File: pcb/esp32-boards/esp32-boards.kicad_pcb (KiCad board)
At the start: 2 copper layers, 55 x 42 mm, 50 parts, among them J1 LCD, J2 USB_B_Micro, J3 BATTERY, Q1 Q_Photo_NPN, SW1 BOOT_MODE, SW2 START, SW3 RESET, SW4 BATTERY_EN, U1 ESP32-C3-WROOM-02, U2 MAX40200AUK, U3 MCP73831-2-OT, U4 LD39150DT33

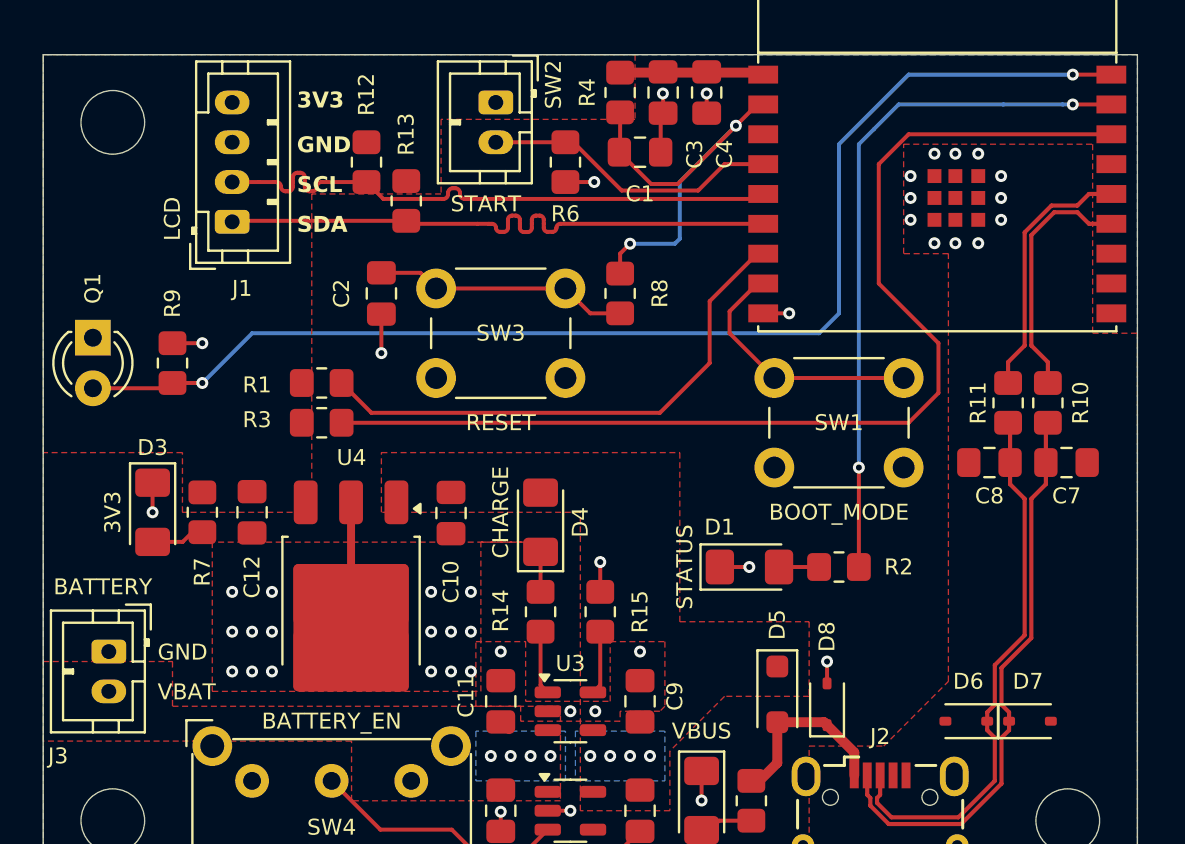
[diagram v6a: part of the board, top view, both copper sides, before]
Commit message: add final touches on silkscreen
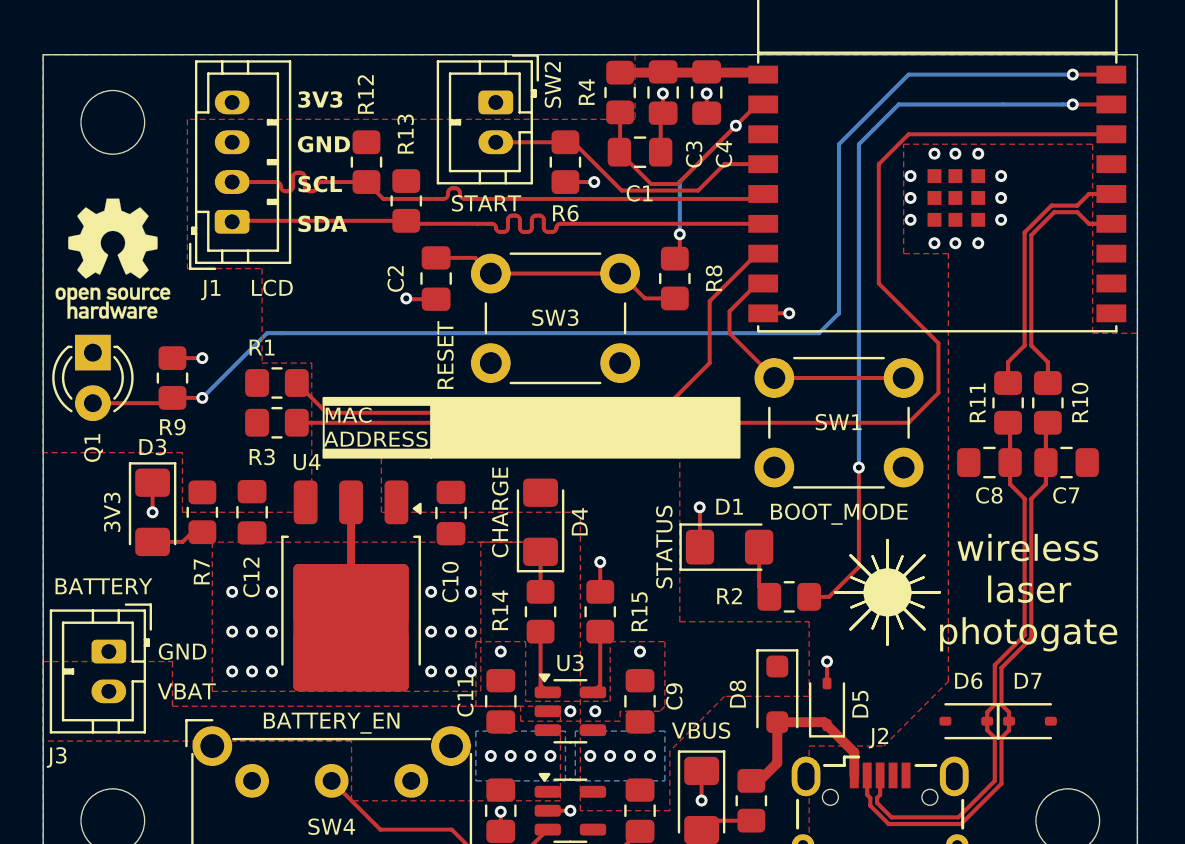
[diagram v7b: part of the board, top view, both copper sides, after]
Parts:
- added REF**: OSHW-Logo_5.7x6mm_SilkScreen, Symbol:OSHW-Logo_5.7x6mm_SilkScreen, F.Cu at (183.0, 105.5)
- added REF**: KiCad-Logo2_5mm_SilkScreen, Symbol:KiCad-Logo2_5mm_SilkScreen, B.Cu at (192.0, 118.2)
- added svg2mod: G***, laser-photogate:laser, F.Cu at (219.2, 119.6)
- moved R2 2.92 mm to (217.0, 122.5)
- moved C2 2.85 mm to (199.2, 106.5)
- moved R8 2.85 mm to (211.2, 106.5)
- moved SW3 2.85 mm to (208.5, 110.8)
- moved R1 2.25 mm to (191.2, 111.8)
- moved R3 2.25 mm to (191.2, 113.8)
- moved D1 1.41 mm to (214.0, 120.0)
- moved Q1 0.75 mm to (182.0, 110.2)
- moved R9 0.75 mm to (186.0, 111.5)
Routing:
- net /EN: track 22.7 -> 19.5 mm
- net /HEARTBEAT: track 34.8 -> 37.9 mm
- net /IO8: track 26.9 -> 29.2 mm
- net /IO2: track 55.7 -> 57.9 mm
- net Net-(D1-A): track 2.01 -> 2.71 mm
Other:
- board text added: "Design files and documentation: https://github.com/tvannoy/laser-photogate/"
- board text added: "MAC ADDRESS"
- board text added: "wireless laser photogate"
- board text added: "© Trevor Vannoy SPDX-License-Identifier: CERN-OHL-S-2.0"

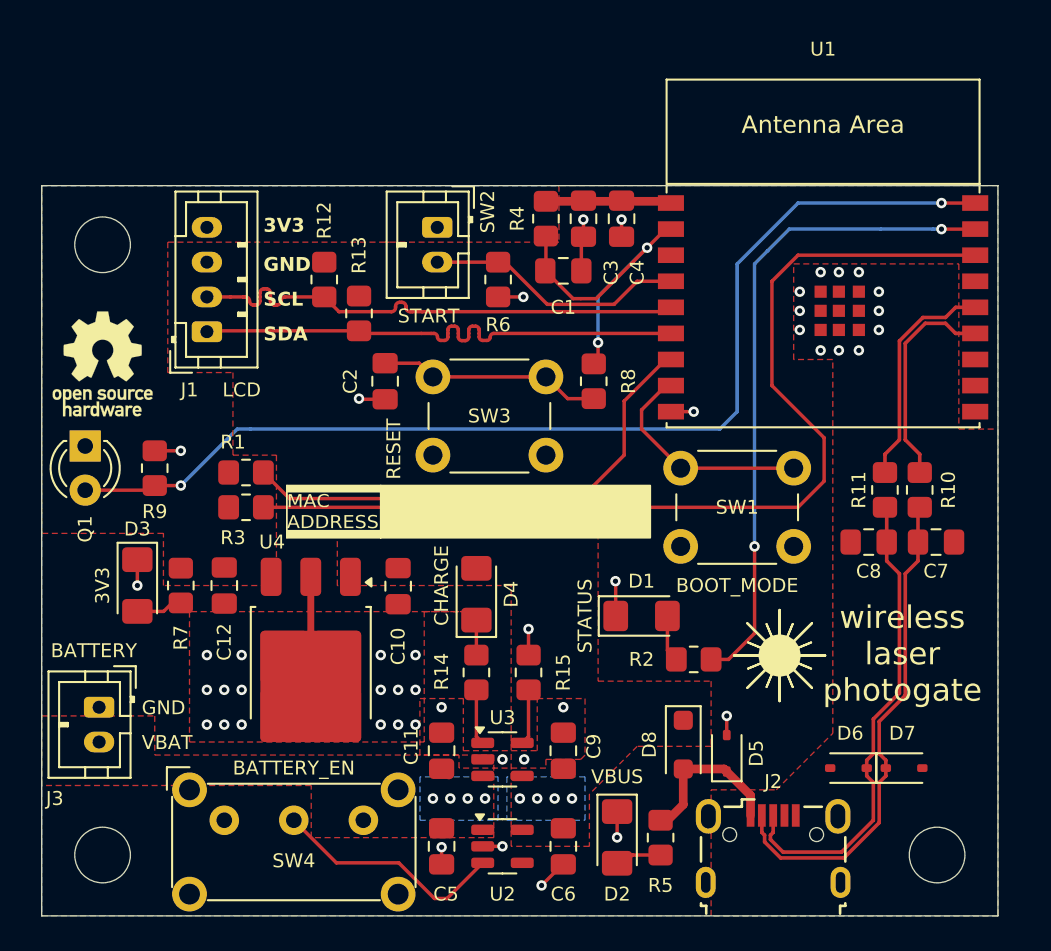
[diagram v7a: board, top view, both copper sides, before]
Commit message: set up DRC and fix DRC errors
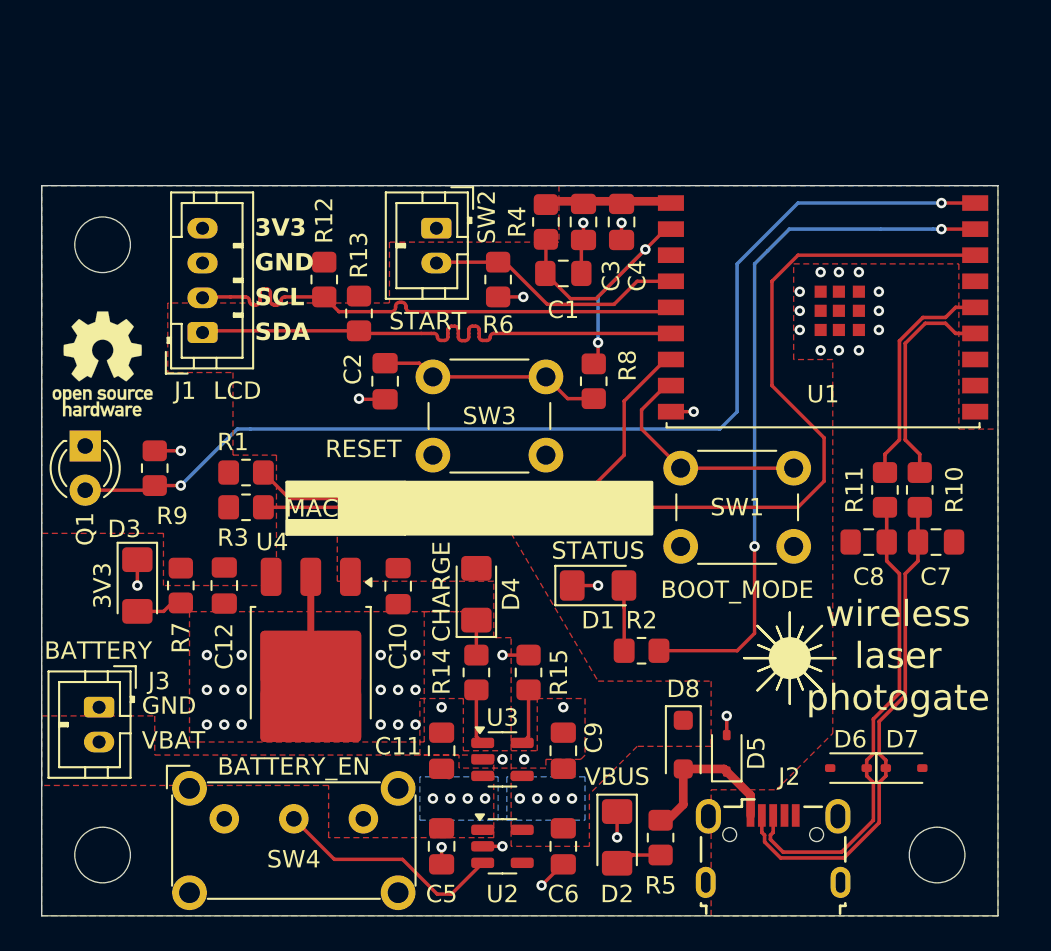
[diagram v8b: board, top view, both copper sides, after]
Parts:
- moved D1 3.05 mm to (211.5, 118.2)
- moved R2 3.04 mm to (214.0, 122.0)
- moved svg2mod 0.60 mm to (219.8, 119.7)
- moved J1 0.25 mm to (188.8, 103.7)
- moved C3 0.19 mm to (210.7, 97.3)
- moved C4 0.19 mm to (212.8, 97.3)
- moved R4 0.19 mm to (208.5, 97.3)
- moved C1 0.15 mm to (209.5, 100.3)
- moved SW4 0.08 mm to (190.0, 131.7)
- moved SW2 0.07 mm to (202.2, 97.7)
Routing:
- net /HEARTBEAT: track 37.9 -> 40.7 mm
- net Net-(D1-A): track 2.71 -> 3.76 mm
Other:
- board text added: "MAC"
- board text removed: "MAC ADDRESS"
